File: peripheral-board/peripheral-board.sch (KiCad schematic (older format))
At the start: 17 parts, among them J1 Power, J2 Arduino Ports, J3 4WD controller, J4 Head, J5 LED1, J6 LED2, M1 UsbToUartX2, Q1 IRLR8113, Q2 IRLR8113

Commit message: First pcb version
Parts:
- added JP1, JP2, JP3: Jumper, Wire_Connections_Bridges:WireConnection_0.80mmDrill, symbol Jumper
- renumbered R8 to R7, R7 to R8
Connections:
- net +5V: now also J1.2 (Pin_2); no longer J1.3 (Pin_3)
- net +7.4V: now also J1.3 (Pin_3); no longer J1.2 (Pin_2)
- net GND: now also R8.2; no longer R8.1
- net at Q1.2 (D): now also JP2.1; no longer J5.1 (Pin_1)
- net at R3.1, R4.2: now also JP1.2; no longer J2.3 (Pin_3)
- new net: JP3.2, R7.2
- new net: J2.2 (Pin_2), JP3.1, R8.1
- new net: J2.3 (Pin_3), JP1.1
- new net: J5.1 (Pin_1), JP2.2
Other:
- moved on the sheet: J5, J6, Q2, R7, R8

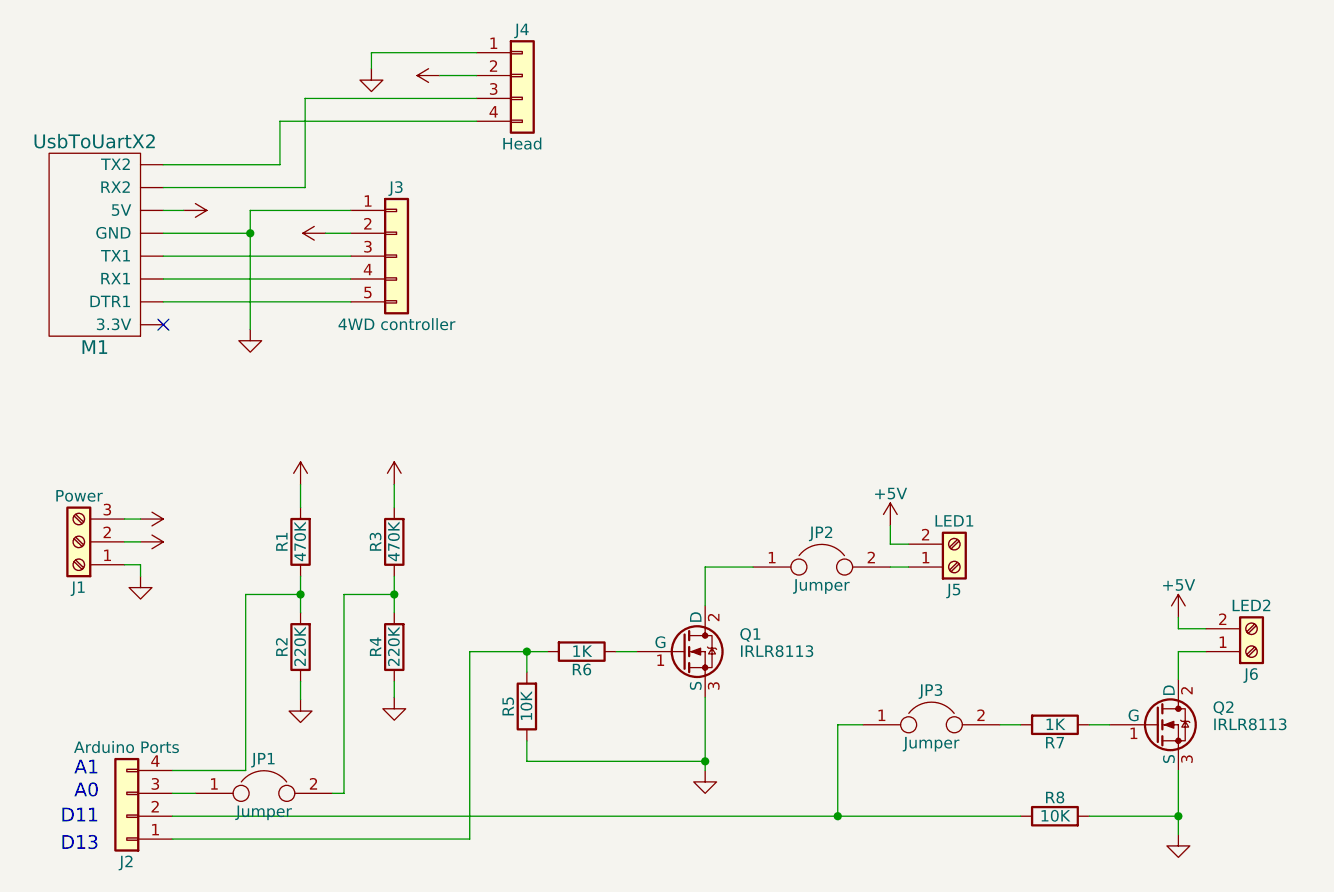
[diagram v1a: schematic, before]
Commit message: Terminal blocks were fixed
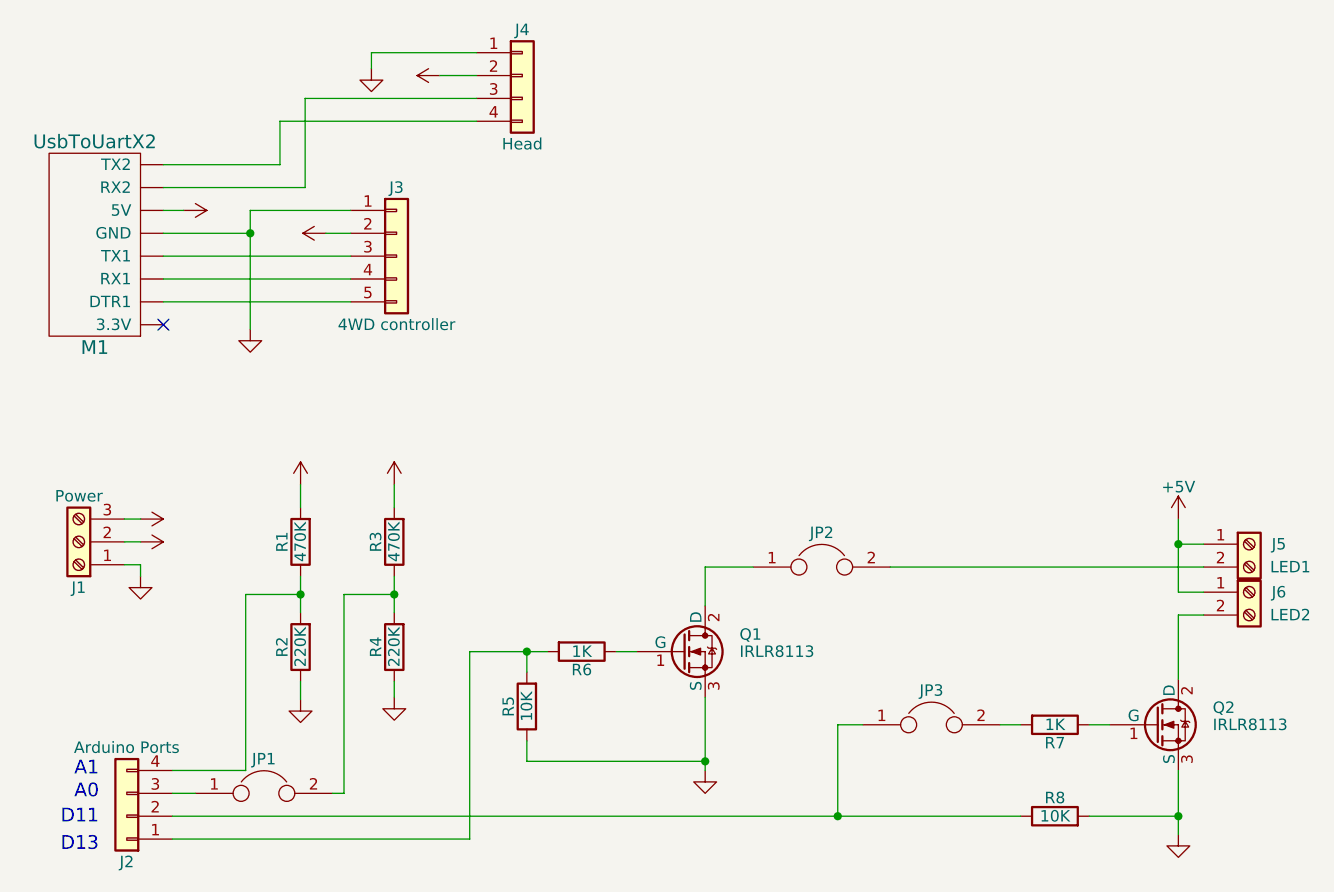
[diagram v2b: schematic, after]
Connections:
- net +5V: now also J5.1 (Pin_1), J6.1 (Pin_1); no longer J5.2 (Pin_2), J6.2 (Pin_2)
- net at Q2.2 (D): now also J6.2 (Pin_2); no longer J6.1 (Pin_1)
- net at JP2.2: now also J5.2 (Pin_2); no longer J5.1 (Pin_1)
